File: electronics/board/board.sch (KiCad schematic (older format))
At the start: 62 parts, among them J1 Conn_02x05_Odd_Even, J2 USB_A, J3 Micro_SD_Card_Det_Hirose_DM3AT, SW1 SW_Push, U1 JW5211, U2 JW5211, U3 JW5211, U4 F1C100s, U5 SST26VF080A-104I/SN, U6 USBLC6-2SC6, U7 ATECC608A-SSHDA, Y1 Crystal_GND24

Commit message: Nearly finished up all the layout, power distrobution done. Just a couple more nets to connect up and silk.
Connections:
- net USB_DM renamed USB_N
- net USB_DP renamed USB_P
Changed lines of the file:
@@
 	6900 5550 6850 5550
 Text Label 6850 5450 2    50   ~ 0
-USB_DP
+USB_P
 Text Label 6850 5550 2    50   ~ 0
-USB_DM
+USB_N
 Text Label 8550 6850 0    50   ~ 0
-USB_DP
+USB_P
 Text Label 8550 7800 0    50   ~ 0
-USB_DM
+USB_N
 $Comp
 L power:GND #PWR032

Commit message: Layout finished, added some images.
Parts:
- removed C1, C10, C21: 100nF, Capacitor_SMD:C_0603_1608Metric, symbol Device:C_Small
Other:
- moved on the sheet: C22
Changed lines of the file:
@@
 Wire Wire Line
 	2250 7900 2200 7850
-$Comp
-L Device:C_Small C10
-U 1 1 60F24B25
-P 2250 8050
-F 0 "C10" H 2050 8100 50  0000 L CNN
-F 1 "100nF" H 2000 7950 50  0000 L CNN
-F 2 "Capacitor_SMD:C_0603_1608Metric" H 2250 8050 50  0001 C CNN
-F 3 "~" H 2250 8050 50  0001 C CNN
-	1    2250 8050
-	1    0    0    -1
-$EndComp
 Connection ~ 2250 7900
 Wire Wire Line
@@
 Connection ~ 3950 7900
 $Comp
-L Device:C_Small C1
-U 1 1 60F6C23F
-P 800 7300
-F 0 "C1" V 700 7350 50  0000 L CNN
-F 1 "100nF" V 700 7050 50  0000 L CNN
-F 2 "Capacitor_SMD:C_0603_1608Metric" H 800 7300 50  0001 C CNN
-F 3 "~" H 800 7300 50  0001 C CNN
-	1    800  7300
-	1    0    0    -1
-$EndComp
-$Comp
 L Device:C_Small C2
 U 1 1 60F70508
@@
 $EndComp
 Wire Wire Line
-	800  7400 800  7600
-Wire Wire Line
-	800  7600 1000 7600
-Wire Wire Line
 	1200 7600 1200 7400
 Wire Wire Line
 	1000 7400 1000 7600
-Connection ~ 1000 7600
 $Comp
 L Device:C_Small C4
@@
 Connection ~ 1200 7600
 Wire Wire Line
-	800  7200 800  7100
-Wire Wire Line
-	800  7100 1000 7100
-Wire Wire Line
 	1400 7100 1400 7200
 Wire Wire Line
@@
 Wire Wire Line
 	1000 7200 1000 7100
-Connection ~ 1000 7100
 $Comp
 L power:+3.3V #PWR03
@@
 Wire Wire Line
 	4900 8350 4900 8550
-$Comp
-L Device:C_Small C21
-U 1 1 610621FE
-P 5300 8250
-F 0 "C21" V 5200 8300 50  0000 L CNN
-F 1 "100nF" V 5200 8000 50  0000 L CNN
-F 2 "Capacitor_SMD:C_0603_1608Metric" H 5300 8250 50  0001 C CNN
-F 3 "~" H 5300 8250 50  0001 C CNN
-	1    5300 8250
-	1    0    0    -1
-$EndComp
-Wire Wire Line
-	5300 8350 5300 8550
-Wire Wire Line
-	5300 8550 5200 8550
-Connection ~ 5100 8550
-Wire Wire Line
-	5300 8050 5300 8150
-Wire Wire Line
-	5100 8150 5100 8050
-Connection ~ 5100 8050
-Wire Wire Line
-	5100 8050 5200 8050
-Wire Wire Line
-	4900 8150 4900 8050
-Wire Wire Line
-	5200 7950 5200 8050
-Wire Wire Line
-	5200 8600 5200 8550
-Wire Wire Line
-	4900 8550 5100 8550
-Wire Wire Line
-	4900 8050 5100 8050
+Wire Wire Line
+	5100 8150 5100 8000
+Wire Wire Line
+	4900 8150 4900 8000
+Wire Wire Line
+	5000 7950 5000 8000
+Wire Wire Line
+	5000 8600 5000 8550
+Wire Wire Line
+	4900 8550 5000 8550
+Wire Wire Line
+	4900 8000 5000 8000
 $Comp
 L Device:C_Small C22
 U 1 1 6106221F
-P 5500 8250
-F 0 "C22" V 5400 8300 50  0000 L CNN
-F 1 "100nF" V 5400 8000 50  0000 L CNN
-F 2 "Capacitor_SMD:C_0603_1608Metric" H 5500 8250 50  0001 C CNN
-F 3 "~" H 5500 8250 50  0001 C CNN
-	1    5500 8250
-	1    0    0    -1
-$EndComp
-Wire Wire Line
-	5500 8550 5500 8350
-Wire Wire Line
-	5500 8150 5500 8050
-Wire Wire Line
-	5300 8050 5500 8050
-Wire Wire Line
-	5300 8550 5500 8550
-Connection ~ 5300 8550
-Connection ~ 5200 8050
-Wire Wire Line
-	5200 8050 5300 8050
-Connection ~ 5200 8550
-Wire Wire Line
-	5200 8550 5100 8550
+P 2250 8050
+F 0 "C22" V 2150 8100 50  0000 L CNN
+F 1 "100nF" V 2150 7800 50  0000 L CNN
+F 2 "Capacitor_SMD:C_0603_1608Metric" H 2250 8050 50  0001 C CNN
+F 3 "~" H 2250 8050 50  0001 C CNN
+	1    2250 8050
+	1    0    0    -1
+$EndComp
 $Comp
 L power:+2V5 #PWR030
 U 1 1 6107EFA0
-P 5200 7950
-F 0 "#PWR030" H 5200 7800 50  0001 C CNN
-F 1 "+2V5" H 5350 8050 50  0000 C CNN
-F 2 "" H 5200 7950 50  0001 C CNN
-F 3 "" H 5200 7950 50  0001 C CNN
-	1    5200 7950
-	1    0    0    -1
-$EndComp
-Connection ~ 5300 8050
+P 5000 7950
+F 0 "#PWR030" H 5000 7800 50  0001 C CNN
+F 1 "+2V5" H 5150 8050 50  0000 C CNN
+F 2 "" H 5000 7950 50  0001 C CNN
+F 3 "" H 5000 7950 50  0001 C CNN
+	1    5000 7950
+	1    0    0    -1
+$EndComp
 Wire Wire Line
 	3250 2150 3450 2350
@@
 L power:GND #PWR031
 U 1 1 61062216
-P 5200 8600
-F 0 "#PWR031" H 5200 8350 50  0001 C CNN
-F 1 "GND" H 5205 8427 50  0001 C CNN
-F 2 "" H 5200 8600 50  0001 C CNN
-F 3 "" H 5200 8600 50  0001 C CNN
-	1    5200 8600
+P 5000 8600
+F 0 "#PWR031" H 5000 8350 50  0001 C CNN
+F 1 "GND" H 5005 8427 50  0001 C CNN
+F 2 "" H 5000 8600 50  0001 C CNN
+F 3 "" H 5000 8600 50  0001 C CNN
+	1    5000 8600
 	1    0    0    -1
 $EndComp
@@
 Text Label 3300 4600 0    50   ~ 0
 1v1_FB
+Connection ~ 5000 8000
+Wire Wire Line
+	5000 8000 5100 8000
+Connection ~ 5000 8550
+Wire Wire Line
+	5000 8550 5100 8550
 $EndSCHEMATC

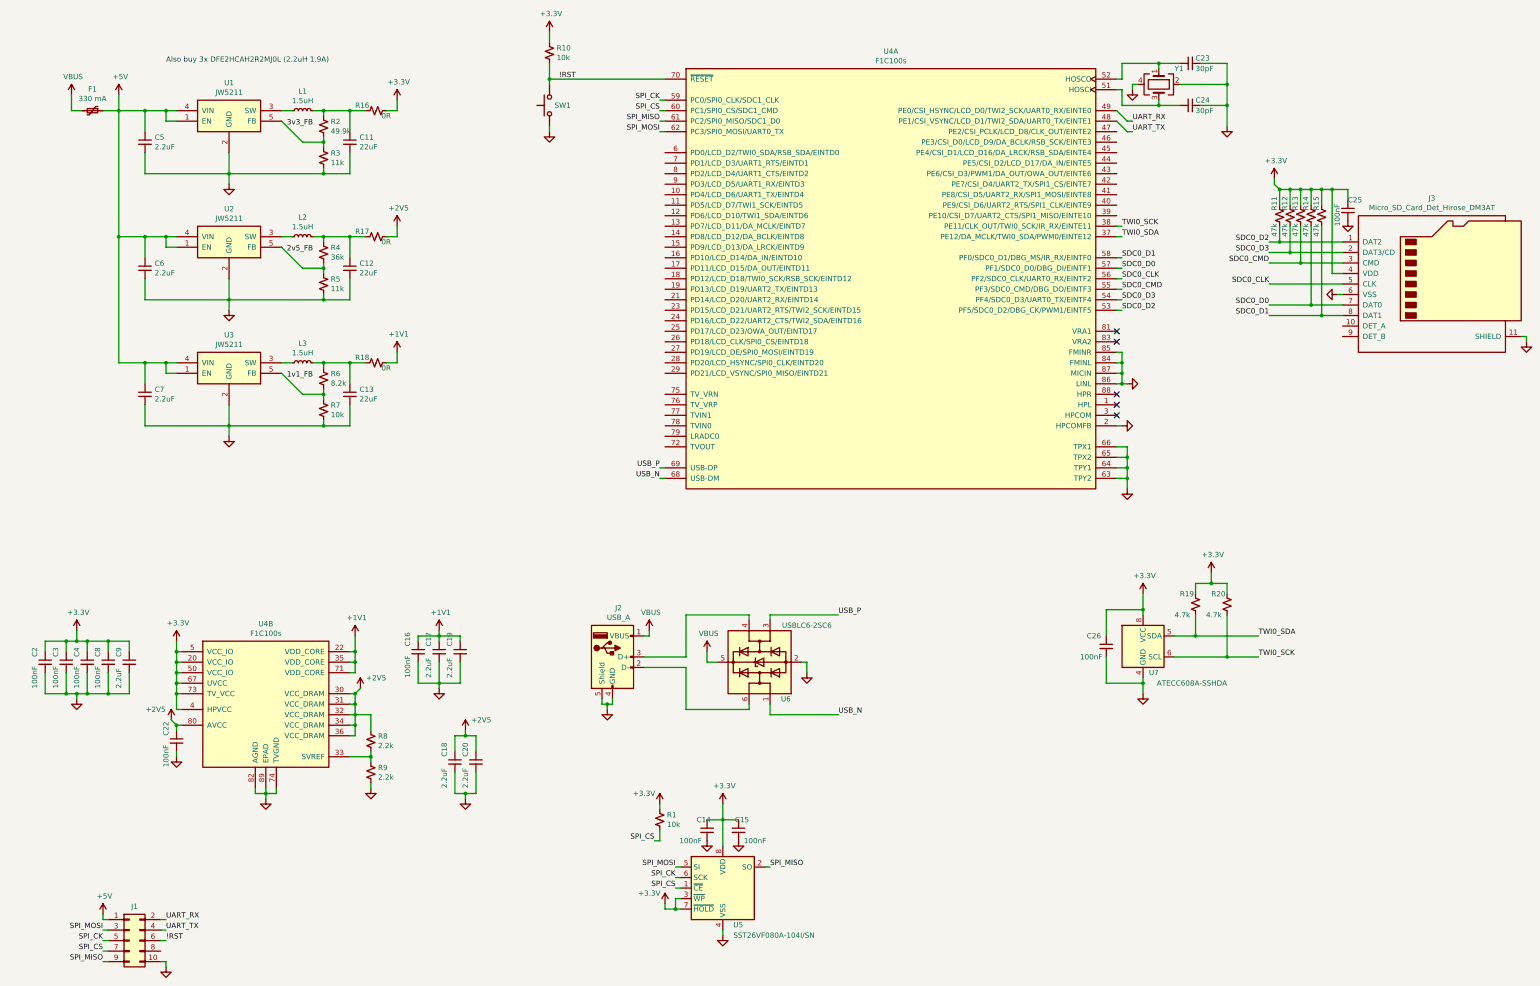
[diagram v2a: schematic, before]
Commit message: Filled in the rest of the part numbers, generated a bom.
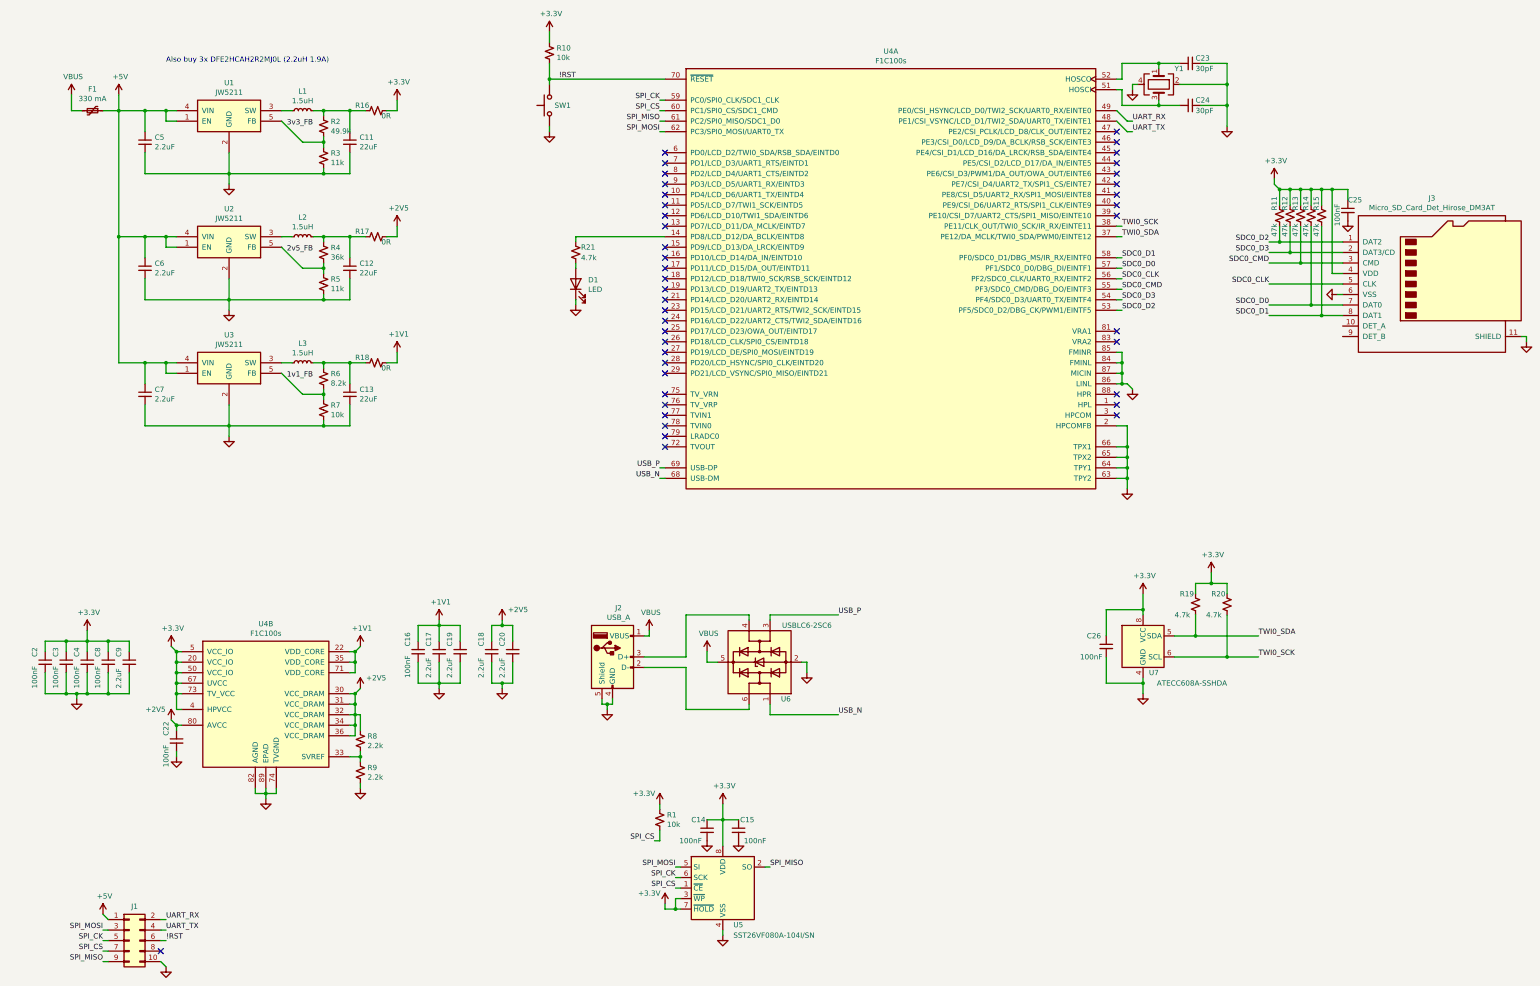
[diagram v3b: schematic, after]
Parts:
- added D1: LED, LED_SMD:LED_0603_1608Metric, symbol Device:LED
- added R21: 4.7k, Resistor_SMD:R_0603_1608Metric, symbol Device:R_Small_US
- C11, C12, C13: MPN (none) -> GRM188R60J226MEA0D
- C14, C15, C16, C2, C25, C26, C3, C4, C8: MPN (none) -> C0603X7R250-104KNP
- C17, C18, C19, C20, C5, C6, C7, C9: MPN (none) -> CL10A225KP8NNNC
- C23, C24: MPN (none) -> GRM1885C1H300JA01D
- J3: MPN (none) -> DM3AT-SF-PEJM5
- R1, R10: MPN (none) -> RC0603FR-0710KL
- R11, R12, R13, R14, R15: MPN (none) -> RC0603FR-0747KL
- R16, R17, R18: MPN (none) -> RC0603FR-070RL
- R19, R20: MPN (none) -> RC0603FR-074K7L
- R2: MPN (none) -> RC0603FR-0749K9
- R3, R5: MPN (none) -> RC0603FR-0711K
- R4: MPN (none) -> RC0603FR-0736K
- R6: MPN (none) -> RC0603FR-078K2L
- R7: MPN (none) -> RC0603FR-0710K
- R8, R9: MPN (none) -> RC0603FR-072K2L
- SW1: MPN (none) -> TL3342F450QG
- U1, U2, U3: MPN (none) -> JW5211
- U4: MPN (none) -> F1C100s
- U6: MPN (none) -> USBLC6-2SC6
- U7: MPN (none) -> ATECC608A-SSHDA
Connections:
- net GND: now also D1.1 (K)
- net at U4.14 (PD8/LCD_D12/DA_BCLK/EINTD8): now also R21.1
- new net: D1.2 (A), R21.2
- no-connect marks 5 -> 42
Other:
- moved on the sheet: C18, C20, R8, R9
